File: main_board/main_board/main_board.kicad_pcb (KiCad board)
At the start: 2 copper layers, 29 parts, among them J1 jstsh5x1, J2 jstsh5x1, J3 jstsh9x1, J4 jstsh9x1, J5 jstsh9x1, J6 jstsh9x1, J7 jstsh4x1, U1 Teensy3.5_All_Pins, U2 TLV2771CDBVT, U3 TLV2771CDBVT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

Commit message: some more layouting of the daugher board
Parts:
- moved H3 61.1 mm to (130.8, 87.6)
- moved H4 51.5 mm to (130.8, 71.1)
- moved H2 32.7 mm to (58.4, 87.6)
- moved H1 16.8 mm to (58.4, 71.1)
- moved U1 9.36 mm to (53.3, 35.6)
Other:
- board outline added: 78.1 x 21.4 mm

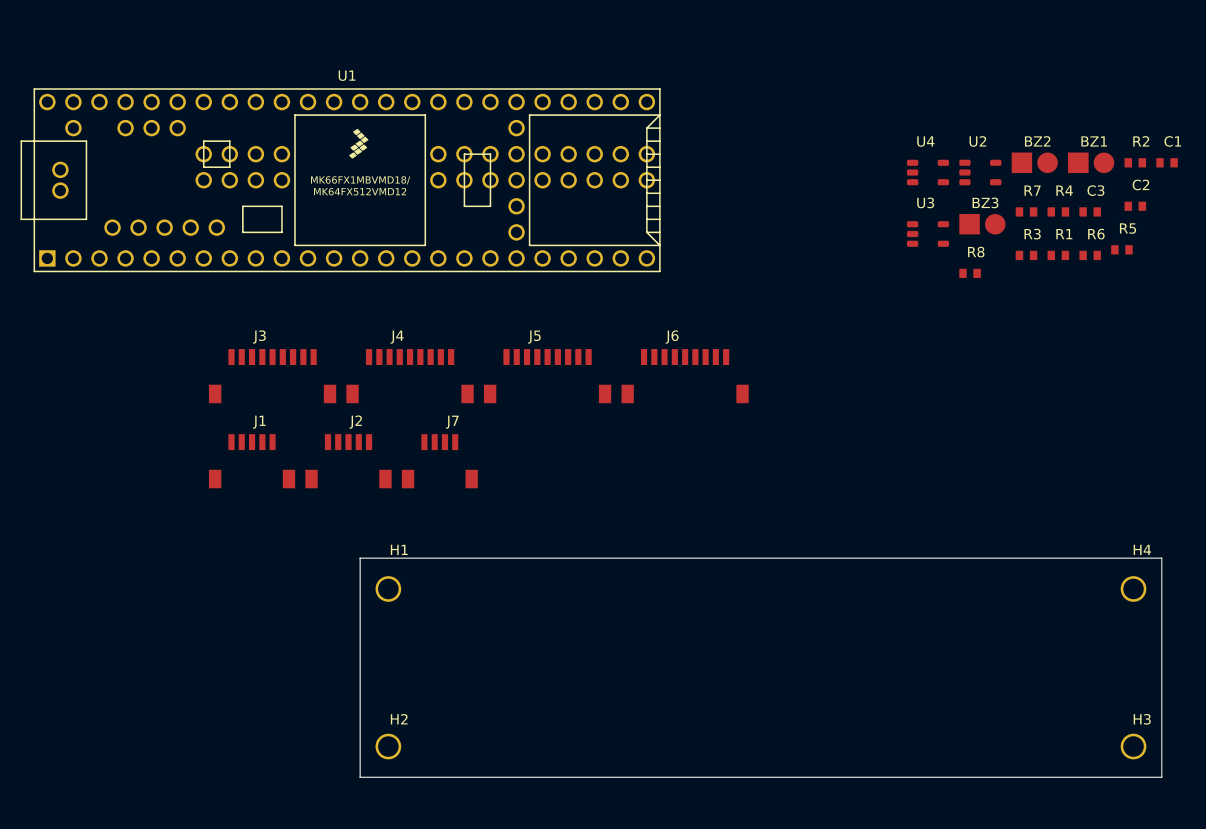
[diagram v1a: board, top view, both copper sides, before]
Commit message: first version of daughter board with pinout
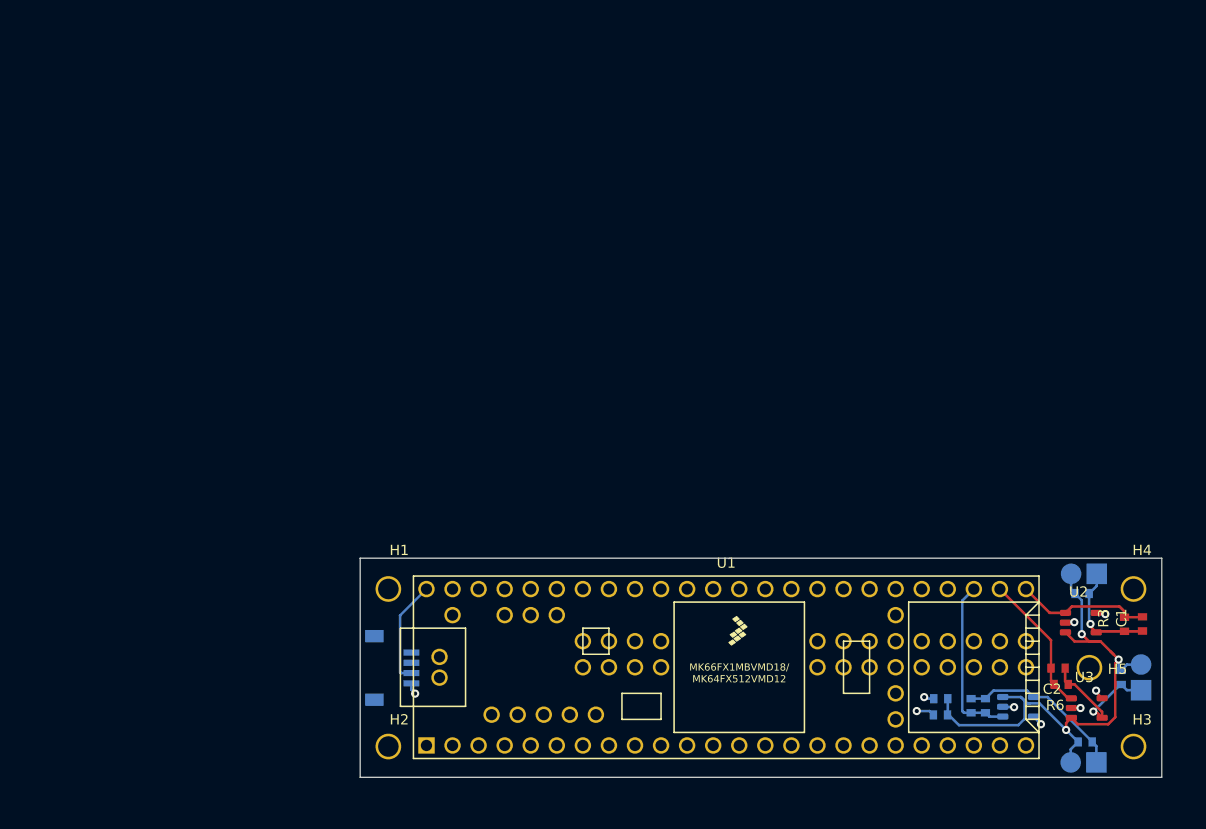
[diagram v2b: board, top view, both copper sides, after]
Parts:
- removed J2: jstsh5x1, exocam_charge_amp:jstsh5x1
- removed J3, J4, J5, J6: jstsh9x1, exocam_charge_amp:jstsh9x1
- removed J7: jstsh4x1, exocam_charge_amp:jstsh4x1
- added H5: MountingHole-Mechanical, exocam_charge_amp:mount_hole_2.5mm, F.Cu at (126.9, 78.9)
- BZ1, BZ2, BZ3, C3, R1, R2, R4, R5, R7, R8, U4: moved to B.Cu
- J1: value jstsh5x1 -> jstsh4x1; footprint exocam_charge_amp:jstsh5x1 -> exocam_charge_amp:jstsh4x1; moved to B.Cu
- moved U1 60.1 mm to (90.3, 83.0)
- moved U4 59.7 mm to (118.5, 90.4)
- moved R7 57.0 mm to (125.8, 92.8)
- moved R2 56.0 mm to (110.6, 83.5), turned to 180 degrees
- moved BZ2 53.9 mm to (133.2, 83.7), turned to 90 degrees
- moved C3 53.3 mm to (111.6, 87.3), turned to 270 degrees
- moved BZ3 53.3 mm to (124.8, 89.8), turned to 180 degrees
- moved R1 51.2 mm to (111.7, 90.2)
- moved C2 50.8 mm to (122.0, 85.6), turned to 180 degrees
- moved U3 48.7 mm to (125.2, 83.5)
- moved C1 47.2 mm to (128.3, 78.2), turned to 90 degrees
- moved R6 47.0 mm to (122.3, 87.2), turned to 180 degrees
- moved R8 45.3 mm to (113.0, 87.3), turned to 270 degrees
- moved U2 44.9 mm to (124.6, 75.2)
- moved R5 44.9 mm to (126.2, 84.6), turned to 270 degrees
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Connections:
- net UNAMP1 renamed Net-(J1-Pad3)
- J1 pad 2: AMP1 -> VBat
- J1 pad 4: +3V3 -> Net-(J1-Pad4)
- U1 pad 27: Net-(U1-Pad27) -> GND
- U1 pad 39: Net-(U1-Pad39) -> GND
- U1 pad 61: Net-(U1-Pad61) -> GND
- U1 pad 62: Net-(U1-Pad62) -> GND
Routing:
- net GND: track 0.00 -> 95.7 mm, vias 0 -> 5
- net +3V3: track 0.00 -> 81.2 mm, vias 0 -> 4
- net VGND: track 0.00 -> 53.8 mm, vias 0 -> 3
- net AMP17: track 0.00 -> 16.5 mm
- net UNAMP17: track 0.00 -> 16.4 mm
- net UNAMP16: track 0.00 -> 13.8 mm, vias 0 -> 1
- net AMP16: track 0.00 -> 13.7 mm
- net AMP15: track 0.00 -> 13.4 mm
- net UNAMP15: track 0.00 -> 10.9 mm, vias 0 -> 1
- net VBat: track 0.00 -> 10.3 mm
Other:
- copper layers 2 -> 4

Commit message: redid daughter board as the time frame and cost was too much with 4 layers (an not really needed).
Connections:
- U1 pad 23: AMP13 -> Net-(U1-Pad23)
- U1 pad 24: AMP14 -> Net-(U1-Pad24)
- U1 pad 31: AMP16 -> AMP6
- U1 pad 32: AMP17 -> AMP7
- U1 pad 33: Net-(U1-Pad33) -> AMP8
- U1 pad 34: Net-(U1-Pad34) -> AMP9
- U1 pad 35: Net-(U1-Pad35) -> AMP10
- U1 pad 36: Net-(U1-Pad36) -> AMP11
- U1 pad 39: GND -> Net-(U1-Pad39)
- U1 pad 45: AMP5 -> AMP12
- U1 pad 46: AMP6 -> AMP13
- U1 pad 47: AMP7 -> AMP14
- U1 pad 48: AMP8 -> Net-(U1-Pad48)
- U1 pad 49: AMP9 -> Net-(U1-Pad49)
- U1 pad 50: AMP10 -> Net-(U1-Pad50)
- U1 pad 56: AMP11 -> Net-(U1-Pad56)
- U1 pad 57: AMP12 -> Net-(U1-Pad57)
- U1 pad 61: GND -> Net-(U1-Pad61)
- U1 pad 62: GND -> Net-(U1-Pad62)
- U1 pad 78: Net-(U1-Pad78) -> AMP16
- U1 pad 79: Net-(U1-Pad79) -> AMP17
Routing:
- net +3V3: track 81.2 -> 139.3 mm
- net GND: track 95.7 -> 42.6 mm, vias 5 -> 3
- net AMP17: track 16.5 -> 13.1 mm, vias 0 -> 1
- net UNAMP15: track 10.9 -> 13.8 mm, vias 1 -> 2
- net AMP16: track 13.7 -> 15.1 mm
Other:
- copper layers 4 -> 2

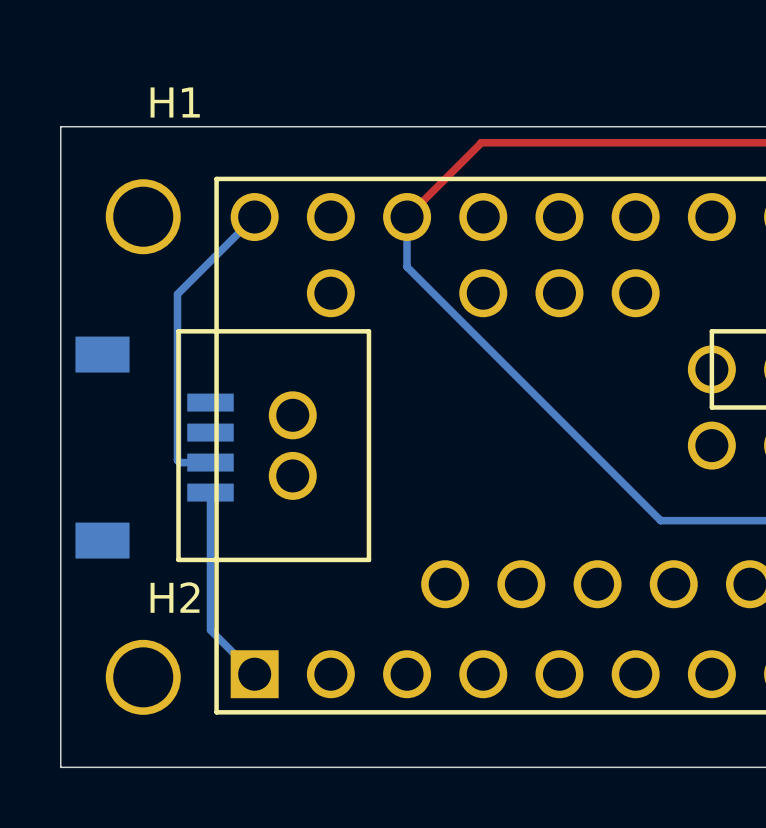
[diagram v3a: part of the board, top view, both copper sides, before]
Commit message: fixed dogbones
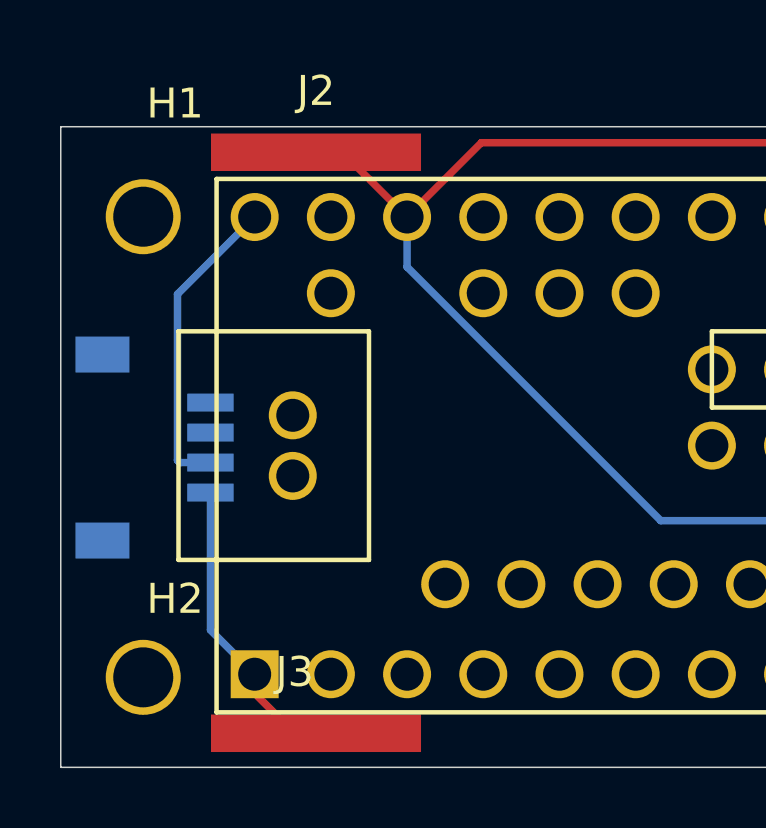
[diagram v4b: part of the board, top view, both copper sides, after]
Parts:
- added J2: 3.3v bus, exocam_charge_amp:power_bus, F.Cu at (63.1, 70.7)
- added J3: GND_bus, exocam_charge_amp:power_bus, F.Cu at (62.4, 90.1)
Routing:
- net +3V3: track 139.3 -> 143.2 mm
- net GND: track 42.6 -> 45.1 mm
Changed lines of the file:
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@@
     (thickness 1.6)
     (drawings 4)
-    (tracks 171)
+    (tracks 175)
     (zones 0)
-    (modules 24)
+    (modules 26)
     (nets 95)
   )
@@
     (mod_text_size 1 1)
     (mod_text_width 0.15)
-    (pad_size 2.5 2.5)
-    (pad_drill 2)
+    (pad_size 7 1.25)
+    (pad_drill 0)
     (pad_to_mask_clearance 0)
     (aux_axis_origin 0 0)
@@
     (add_net VGND)
   )
+  (module exocam_charge_amp:power_bus (layer F.Cu)
+    (at 62.4078 90.0684)
+    (fp_text reference J3 (at 0 0.5) (layer F.SilkS)
+      (effects (font (size 1 1) (thickness 0.15)))
+    )
+    (fp_text value GND_bus (at 0 -0.5) (layer F.Fab)
+      (effects (font (size 1 1) (thickness 0.15)))
+    )
+    (pad 1 smd rect (at 0.7112 2.54) (size 7 1.25) (layers F.Cu F.Paste F.Mask)
+      (net 11 GND))
+  )
+  (module exocam_charge_amp:power_bus (layer F.Cu)
+    (at 63.119 70.7009)
+    (fp_text reference J2 (at 0 0.5) (layer F.SilkS)
+      (effects (font (size 1 1) (thickness 0.15)))
+    )
+    (fp_text value "3.3v bus" (at 0 -0.5) (layer F.Fab)
+      (effects (font (size 1 1) (thickness 0.15)))
+    )
+    (pad 1 smd rect (at 0 2.54) (size 7 1.25) (layers F.Cu F.Paste F.Mask)
+      (net 9 +3V3))
+  )
   (module exocam_charge_amp:mount_hole_2.5mm (layer F.Cu)
     (at 126.9492 78.8797)
@@
   (segment (start 106.084297 86.514899) (end 106.317399 86.748001) (width 0.25) (layer B.Cu) (net 9))
   (segment (start 125.1839 72.9234) (end 68.6308 72.9234) (width 0.25) (layer F.Cu) (net 9))
+  (segment (start 63.9953 73.2409) (end 63.119 73.2409) (width 0.25) (layer F.Cu) (net 9))
+  (segment (start 66.1543 75.3999) (end 63.9953 73.2409) (width 0.25) (layer F.Cu) (net 9))
   (segment (start 123.7919 86.8705) (end 123.9139 86.9925) (width 0.25) (layer F.Cu) (net 11))
   (segment (start 110.5027 86.0806) (end 109.728 86.0806) (width 0.25) (layer B.Cu) (net 11))
@@
   (segment (start 123.806001 79.025699) (end 123.806001 85.993101) (width 0.25) (layer B.Cu) (net 11))
   (segment (start 124.206 78.6257) (end 123.806001 79.025699) (width 0.25) (layer B.Cu) (net 11))
+  (segment (start 61.0743 91.2749) (end 62.4078 92.6084) (width 0.25) (layer F.Cu) (net 11))
+  (segment (start 61.0743 90.6399) (end 61.0743 91.2749) (width 0.25) (layer F.Cu) (net 11))
   (segment (start 58.501099 77.973101) (end 61.0743 75.3999) (width 0.25) (layer B.Cu) (net 24))
   (segment (start 58.501099 83.510299) (end 58.501099 77.973101) (width 0.25) (layer B.Cu) (net 24))

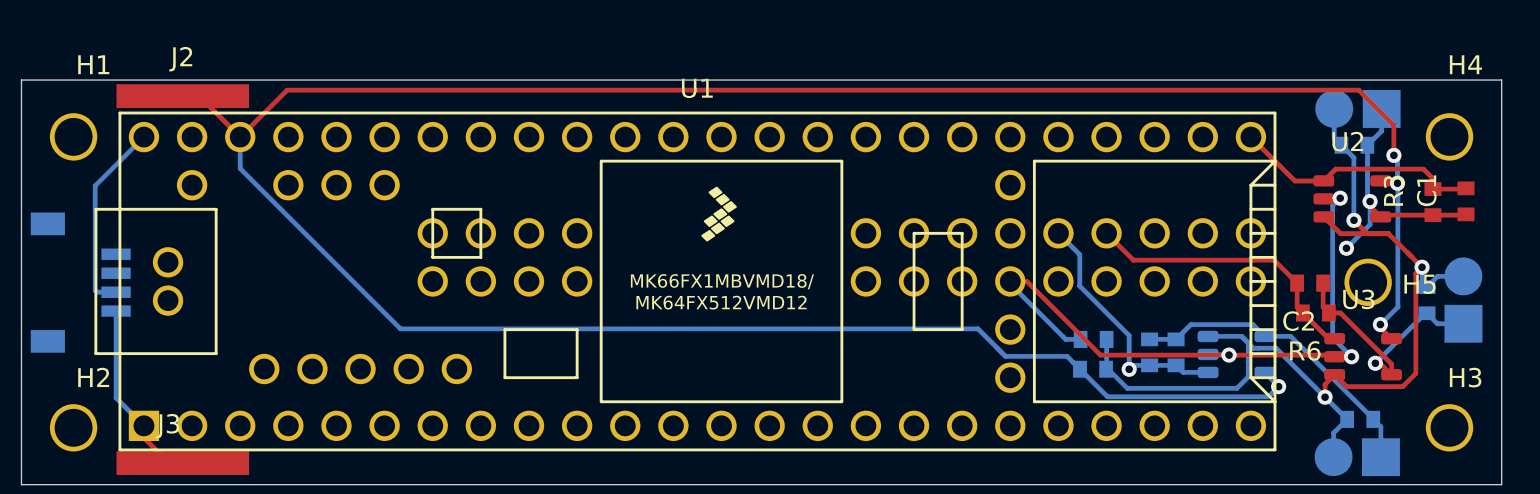
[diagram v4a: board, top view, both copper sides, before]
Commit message: updated daughter board schematic
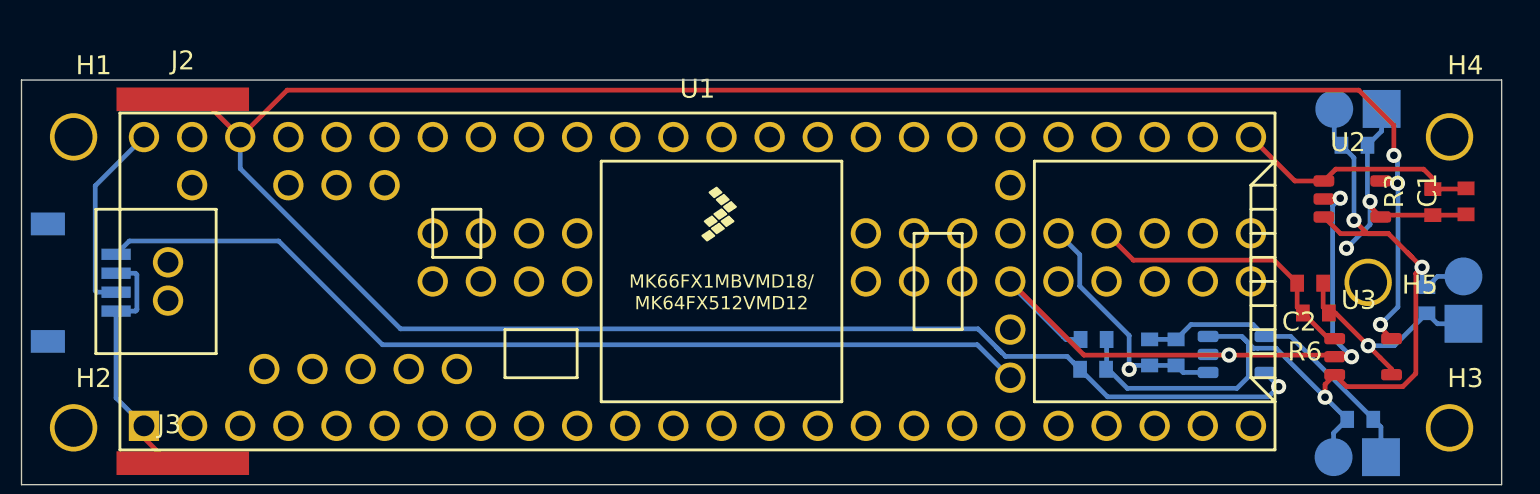
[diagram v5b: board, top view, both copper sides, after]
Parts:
- moved J2 0.17 mm to (63.1, 70.9)
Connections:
- net VBat renamed BAT
- J1 pad 3: Net-(J1-Pad3) -> GND
- J1 pad 4: Net-(J1-Pad4) -> RTCBat
- U1 pad 25: Net-(U1-Pad25) -> RTCBat
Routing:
- net RTCBat: track 0.00 -> 50.5 mm
- net GND: track 45.1 -> 49.2 mm
- net UNAMP16: track 13.8 -> 12.7 mm
- net +3V3: track 143.2 -> 144.0 mm

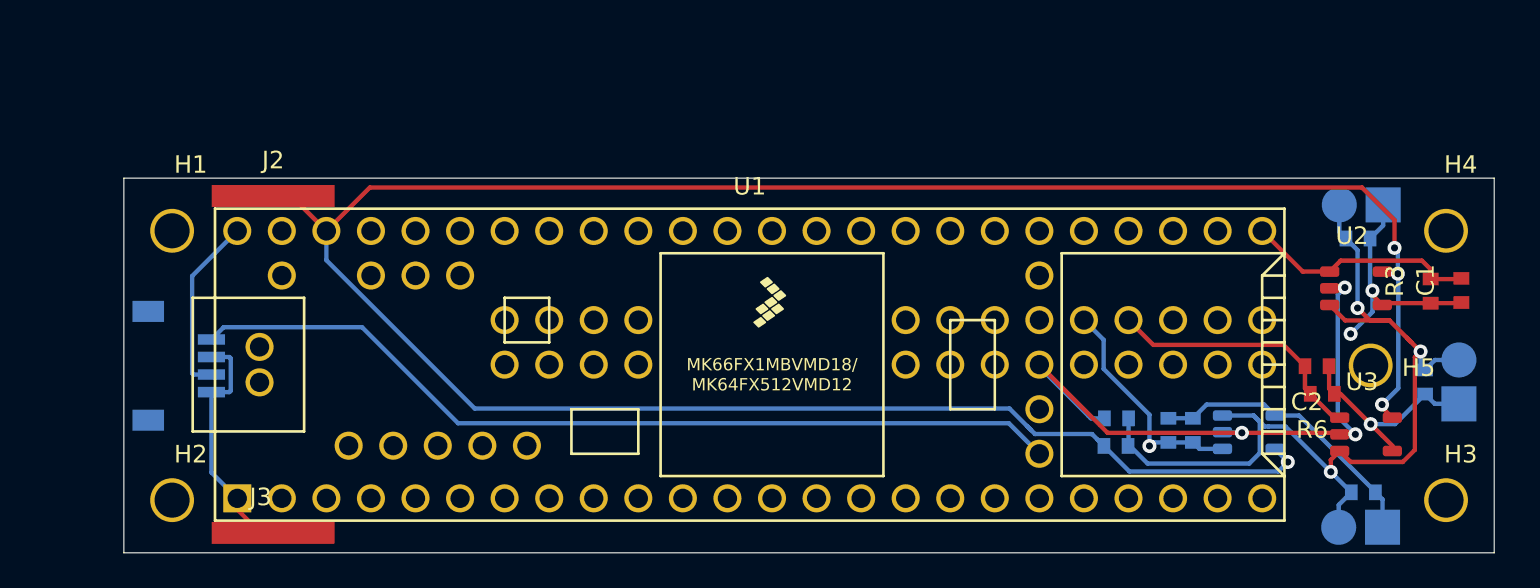
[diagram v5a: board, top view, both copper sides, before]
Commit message: updated daughter board holes, should be good to fab
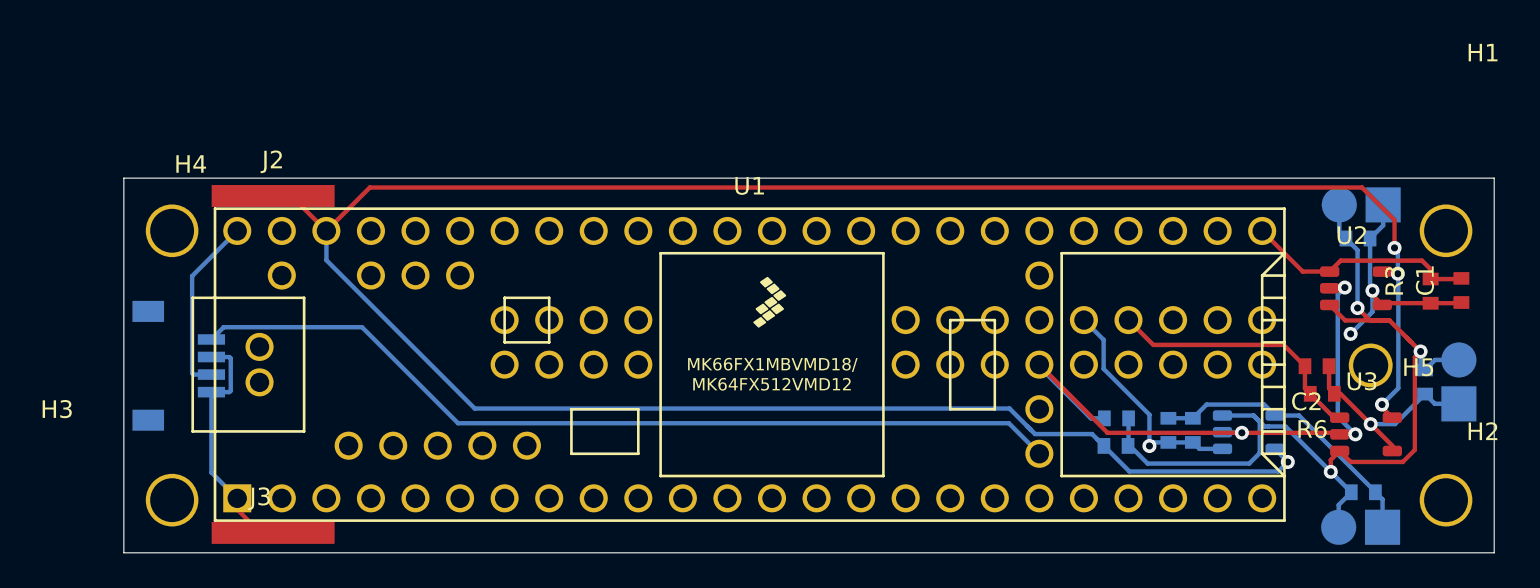
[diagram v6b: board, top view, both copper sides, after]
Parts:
- H1, H2, H3, H4: footprint exocam_charge_amp:mount_hole_2.5mm -> exocam_charge_amp:mount_hole_3mm
- moved H3 80.1 mm to (50.8, 85.1)
- moved H1 73.9 mm to (132.1, 64.8)
- moved H2 73.7 mm to (132.1, 86.4)
- moved H4 72.4 mm to (58.4, 71.1)

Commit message: adjusting hole patterns
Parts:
- moved J2 2.82 mm to (64.8, 68.6)
- moved J3 2.64 mm to (62.4, 92.7)
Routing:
- net GND: track 49.2 -> 53.5 mm
- net UNAMP15: track 13.8 -> 10.9 mm, vias 2 -> 1
- net +3V3: track 144.0 -> 142.8 mm, vias 4 -> 3
- net AMP17: track 13.1 -> 12.2 mm, vias 1 -> 0
- net RTCBat: track 50.5 -> 51.2 mm
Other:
- board size 78.1 x 21.4 mm -> 78.1 x 27.4 mm

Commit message: updated pinout for daughter board (changed pin for AMP3)
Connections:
- net Net-(U1-Pad56) renamed AMP5
